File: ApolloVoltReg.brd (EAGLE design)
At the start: 45.4 x 27.3 mm, 24 parts, among them IC2 LM324D, J1 SSM-108-L-DV-BE-K-APOLLO, U1 TEXAS_INSTRUMENTS_PTH04070WAD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, U2 ACS712ELCTR-05B-T

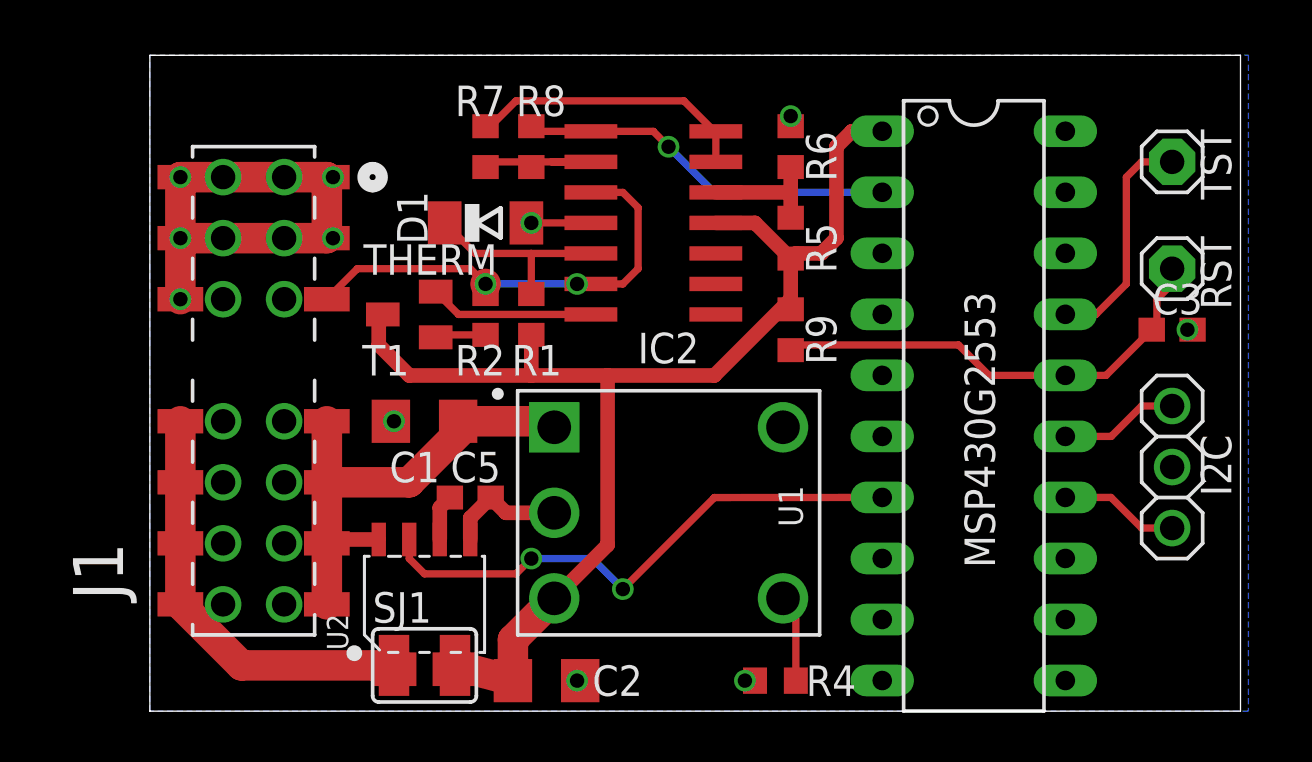
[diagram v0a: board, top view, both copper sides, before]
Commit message: pcb cleanup overtemp-shutdown (optional) gerber files
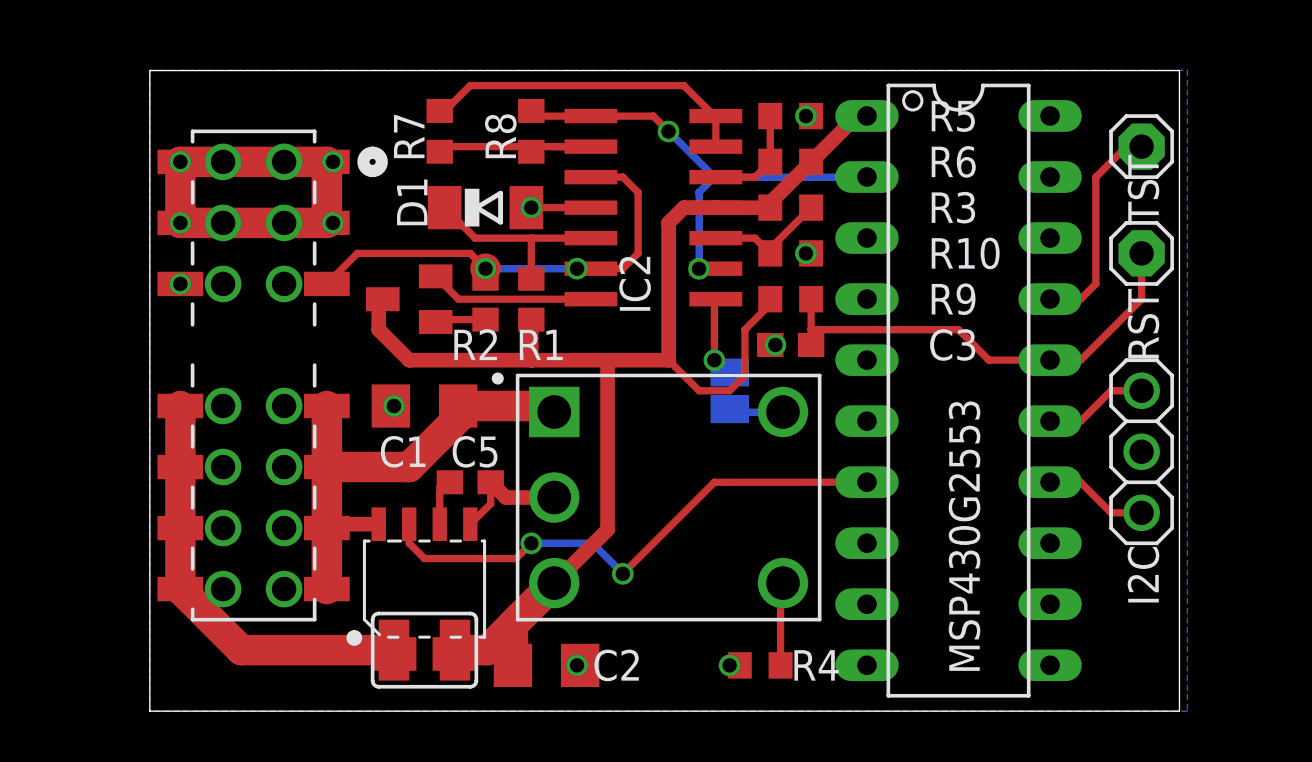
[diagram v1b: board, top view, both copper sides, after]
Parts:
- added R10, R3: 2k8, resistor:R0603
- added SJ2: (no value), jumper:SJ
- moved C3 15.9 mm to (27.9, 15.2), turned to 180 degrees
- moved R5 3.18 mm to (27.9, 22.9), turned to 180 degrees
- moved R7 2.01 mm to (13.3, 24.1)
- moved RST 1.42 mm to (42.5, 19.1)
- moved TST 1.42 mm to (42.5, 23.5)
- moved I2C 1.42 mm to (42.5, 10.8)
- moved R6 1.27 mm to (27.9, 24.8), turned to 0 degrees
- moved R9 1.27 mm to (27.9, 17.1), turned to 0 degrees
- moved MSP430G2553 0.90 mm to (34.9, 13.3)
- moved R4 0.90 mm to (26.7, 1.91)
- moved C2 0.64 mm to (17.8, 1.91)
- moved SJ1 0.64 mm to (12.7, 2.54)
- moved C1 0.63 mm to (12.7, 12.7)
- moved C5 0.63 mm to (14.6, 9.53)
- moved J1 0.63 mm to (2.54, 5.08)
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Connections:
- removed net NC: U1.5
- new net /INHIBIT: SJ2.2, U1.5
- new net N$11: IC2.3, R10.2, R3.1
- new net N$12: IC2.1, SJ2.1
- new net THERM0: J1.6
- net GND: now also R10.1; no longer J1.6
- net TEMPSENS: now also IC2.2
- net VCC: now also R3.2
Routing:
- net VCC: track 52.5 -> 59.2 mm
- net N$11: track 0.00 -> 5.14 mm
- net TEMPSENS: track 15.7 -> 19.2 mm, vias 1 -> 2
- net N$12: track 0.00 -> 3.26 mm, vias 0 -> 1
- net GND: track 27.5 -> 25.0 mm
- net /INHIBIT: track 0.00 -> 2.27 mm
- net N$8: track 6.10 -> 8.01 mm
- net N$7: track 11.8 -> 13.7 mm
- net N$6: track 5.23 -> 4.43 mm
- net SCL: track 4.97 -> 4.34 mm
- net SDA: track 4.97 -> 4.33 mm
- net N$10: track 9.68 -> 9.04 mm
- net ACS_OUT: track 23.1 -> 22.5 mm
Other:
- board size 45.4 x 27.3 mm -> 42.8 x 26.7 mm
- board text added: "Apollo 1260 3.3V/3A MC68060 switching mode voltage reg ©2019 Szymon Biegański github.com/sq7bti/ApolloVR"

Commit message: replace opamp with TL084D
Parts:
- IC2: value LM324D -> TL084D
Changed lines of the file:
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@@
 <attribute name="VALUE" x="25.4" y="2.54" size="1.27" layer="27"/>
 </element>
-<element name="IC2" library="linear" package="SO14" value="LM324D" x="22.225" y="20.955" smashed="yes" rot="R90">
+<element name="IC2" library="linear" package="SO14" value="TL084D" x="22.225" y="20.955" smashed="yes" rot="R90">
 <attribute name="NAME" x="22.098" y="16.51" size="1.27" layer="25" rot="R90"/>
 <attribute name="VALUE" x="23.622" y="16.51" size="1.27" layer="27" rot="R90"/>

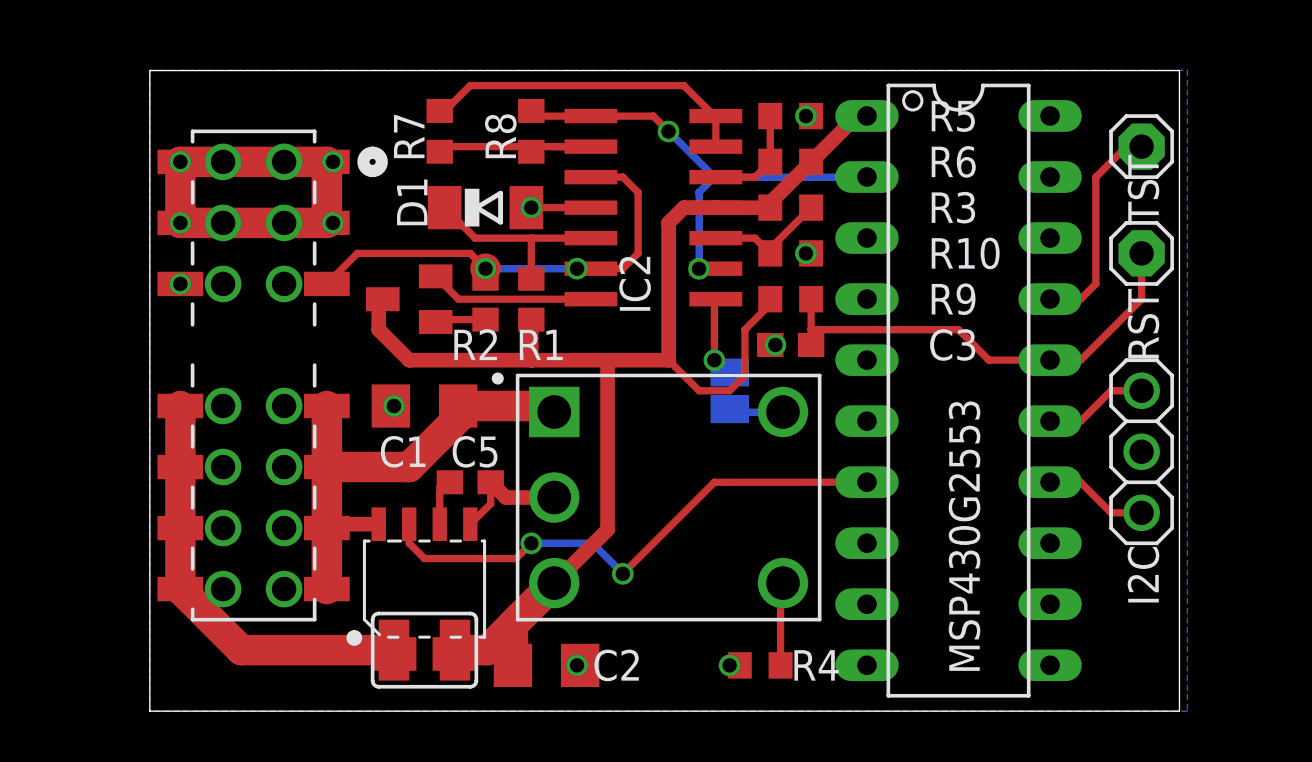
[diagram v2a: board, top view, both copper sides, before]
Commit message: widen high current traces
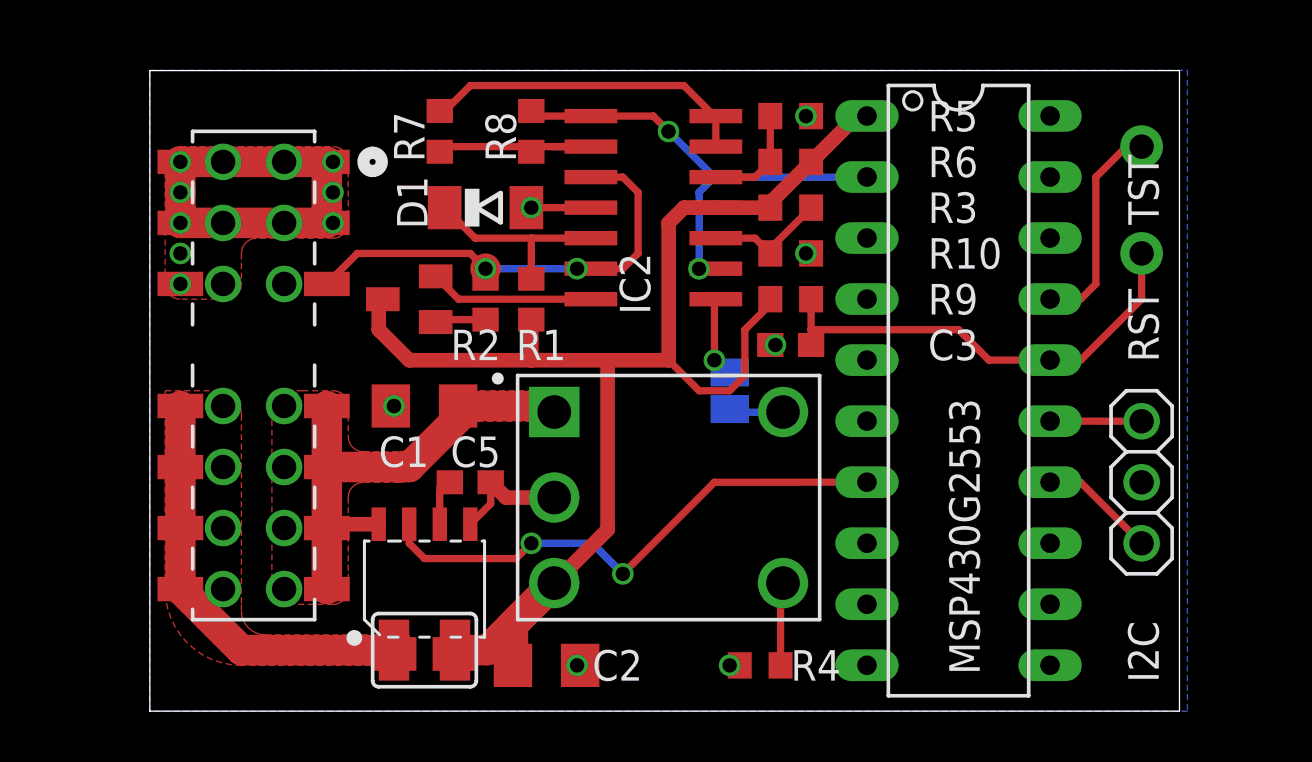
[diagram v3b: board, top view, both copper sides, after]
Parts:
- C5: value (none) -> 100n
- R10: value 2k8 -> 20k
- R2: value (none) -> 840
- R3: value 2k8 -> 2k
- RST, TST: device adafruit:1X01 -> adafruit:1X01-CLEANBIG
- moved I2C 1.27 mm to (42.5, 9.53)
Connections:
- removed net THERM0: J1.6
- net +5V: now also J1.29, J1.31, J1.33, J1.35
- net CPU: now also J1.30, J1.32, J1.34, J1.36
- net GND: now also J1.21, J1.22, J1.23, J1.24, J1.26, J1.6
- net THERM1: now also J1.25
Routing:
- net SCL: track 4.34 -> 4.86 mm
- net SDA: track 4.33 -> 3.81 mm
- net GND: vias 11 -> 15
- added copper zone on layer 1, net +5V
- added copper zone on layer 1, net CPU
- added copper zone on layer 1, net GND

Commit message: gerber in archs
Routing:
- net THERM1: track 18.6 -> 20.4 mm
- net N$8: track 8.01 -> 6.38 mm
- net VCC: track 59.2 -> 60.7 mm
- net CPU: track 17.6 -> 19.0 mm
- net N$12: track 3.26 -> 4.11 mm
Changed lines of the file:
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@@
 <grid distance="0.025" unitdist="inch" unit="inch" style="lines" multiple="1" display="yes" altdistance="0.025" altunitdist="inch" altunit="inch"/>
 <layers>
-<layer number="1" name="Top" color="4" fill="1" visible="yes" active="yes"/>
-<layer number="16" name="Bottom" color="1" fill="1" visible="yes" active="yes"/>
+<layer number="1" name="Top" color="4" fill="1" visible="no" active="yes"/>
+<layer number="16" name="Bottom" color="1" fill="1" visible="no" active="yes"/>
 <layer number="17" name="Pads" color="2" fill="1" visible="yes" active="yes"/>
 <layer number="18" name="Vias" color="2" fill="1" visible="yes" active="yes"/>
@@
 ©2019 Szymon Biegański
 github.com/sq7bti/ApolloVR</text>
+<dimension x1="1.27" y1="0" x2="44.45" y2="0" x3="22.86" y3="-3.175" textsize="1.778" layer="20" dtype="horizontal"/>
+<dimension x1="1.27" y1="0" x2="1.27" y2="26.67" x3="-1.27" y3="13.335" textsize="1.778" layer="20" dtype="horizontal"/>
 </plain>
 <attributes>
@@
 <contactref element="THERM" pad="TP"/>
 <contactref element="J1" pad="25"/>
+<wire x1="6.858" y1="17.78" x2="8.636" y2="17.78" width="0.4064" layer="1"/>
 <wire x1="19.05" y1="18.415" x2="19.625" y2="18.415" width="0" layer="19" extent="1-1"/>
-<wire x1="6.858" y1="17.78" x2="8.636" y2="17.78" width="0" layer="19" extent="1-1"/>
 </signal>
 <signal name="+5V">
@@
 <contactref element="R7" pad="2"/>
 <contactref element="R8" pad="1"/>
-<wire x1="19.625" y1="23.495" x2="17.995" y2="23.495" width="0.3048" layer="1"/>
-<wire x1="19.625" y1="23.495" x2="13.55" y2="23.495" width="0.3048" layer="1"/>
-<wire x1="13.55" y1="23.495" x2="13.335" y2="23.28" width="0.3048" layer="1"/>
-<wire x1="17.995" y1="23.495" x2="17.145" y2="23.28" width="0" layer="19" extent="1-1"/>
+<wire x1="13.335" y1="23.28" x2="17.145" y2="23.28" width="0.4064" layer="1"/>
+<wire x1="17.145" y1="23.28" x2="18.2" y2="23.28" width="0.4064" layer="1"/>
+<wire x1="18.2" y1="23.28" x2="18.415" y2="23.495" width="0.4064" layer="1"/>
+<wire x1="18.415" y1="23.495" x2="19.625" y2="23.495" width="0.4064" layer="1"/>
 </signal>
 <signal name="TEMPSENS">
@@
 <contactref element="IC2" pad="8"/>
 <contactref element="MSP430G2553" pad="2"/>
-<wire x1="19.625" y1="24.765" x2="17.36" y2="24.765" width="0.3048" layer="1"/>
-<wire x1="17.36" y1="24.765" x2="17.145" y2="24.98" width="0.3048" layer="1"/>
 <wire x1="19.625" y1="24.765" x2="22.225" y2="24.765" width="0.3048" layer="1"/>
 <wire x1="22.225" y1="24.765" x2="22.855" y2="24.125" width="0.3048" layer="1"/>
@@
 <wire x1="24.755" y1="22.225" x2="24.125" y2="21.595" width="0.3048" layer="16"/>
 <wire x1="24.125" y1="21.595" x2="24.125" y2="18.41" width="0.3048" layer="16"/>
+<wire x1="19.625" y1="24.765" x2="17.36" y2="24.765" width="0.4064" layer="1"/>
+<wire x1="17.36" y1="24.765" x2="17.145" y2="24.98" width="0.4064" layer="1"/>
 <wire x1="24.125" y1="18.41" x2="24.825" y2="18.415" width="0" layer="19" extent="1-1"/>
 </signal>
@@
 <wire x1="17.145" y1="16.295" x2="17.145" y2="14.605" width="0.6096" layer="1"/>
 <wire x1="20.32" y1="14.605" x2="22.86" y2="14.605" width="0.6096" layer="1"/>
-<wire x1="13.97" y1="2.54" x2="15.31" y2="2.54" width="1.27" layer="1"/>
-<wire x1="15.31" y1="2.54" x2="18.45" y2="5.68" width="1.27" layer="1"/>
+<wire x1="13.97" y1="2.54" x2="15.31" y2="2.54" width="1.6764" layer="1"/>
+<wire x1="15.31" y1="2.54" x2="18.45" y2="5.68" width="1.6764" layer="1"/>
 <contactref element="R3" pad="2"/>
 <wire x1="24.825" y1="20.955" x2="23.495" y2="20.955" width="0.6096" layer="1"/>
@@
 <wire x1="25.4" y1="13.335" x2="24.13" y2="13.335" width="0.3048" layer="1"/>
 <wire x1="24.13" y1="13.335" x2="22.86" y2="14.605" width="0.3048" layer="1"/>
-<wire x1="13.335" y1="2.38" x2="13.97" y2="2.54" width="0" layer="19" extent="1-1"/>
-<wire x1="14.605" y1="2.38" x2="13.97" y2="2.54" width="0" layer="19" extent="1-1"/>
+<wire x1="13.335" y1="2.38" x2="13.97" y2="2.38" width="0.4064" layer="1"/>
+<wire x1="14.605" y1="2.38" x2="13.97" y2="2.38" width="0.4064" layer="1"/>
+<wire x1="13.97" y1="2.38" x2="13.97" y2="2.54" width="0.4064" layer="1"/>
 </signal>
 <signal name="CPU">
@@
 <wire x1="2.54" y1="12.7" x2="2.54" y2="5.08" width="1.27" layer="1"/>
 <wire x1="2.54" y1="5.08" x2="5.08" y2="2.54" width="1.27" layer="1"/>
-<wire x1="5.08" y1="2.54" x2="11.43" y2="2.54" width="1.27" layer="1"/>
+<wire x1="5.08" y1="2.54" x2="11.43" y2="2.54" width="1.6764" layer="1"/>
 <polygon width="0.4064" layer="1">
 <vertex x="1.905" y="13.335"/>
@@
 <contactref element="J1" pad="34"/>
 <contactref element="J1" pad="36"/>
-<wire x1="11.43" y1="2.54" x2="10.795" y2="2.38" width="0" layer="19" extent="1-1"/>
-<wire x1="12.065" y1="2.38" x2="11.43" y2="2.54" width="0" layer="19" extent="1-1"/>
+<wire x1="10.795" y1="2.38" x2="11.43" y2="2.38" width="0.4064" layer="1"/>
+<wire x1="12.065" y1="2.38" x2="11.43" y2="2.38" width="0.4064" layer="1"/>
+<wire x1="11.43" y1="2.38" x2="11.43" y2="2.54" width="0.4064" layer="1"/>
 </signal>
 <signal name="N$9">
@@
 <wire x1="24.765" y1="14.605" x2="24.765" y2="17.085" width="0.3048" layer="1"/>
 <wire x1="24.765" y1="17.085" x2="24.825" y2="17.145" width="0.3048" layer="1"/>
-<wire x1="24.765" y1="14.605" x2="25.4" y2="14.097" width="0" layer="19" extent="16-16"/>
+<wire x1="25.4" y1="14.097" x2="25.273" y2="14.097" width="0.4064" layer="16"/>
+<wire x1="25.273" y1="14.097" x2="24.765" y2="14.605" width="0.4064" layer="16"/>
 </signal>
 </signals>

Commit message: adding pic
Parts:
- removed T1: (no value), transistor:SOT23-EBC
- added D2: BAS40-06, diode:SOT23
- added FAN: (no value), pinhead:1X02
- added IC1: MCP1703CB, linear:SOT23
- added LED1: (no value), adafruit:LED3MM
- added Q1: (no value), semicon-smd-ipc:SOT23
- added Q2: (no value), adafruit:SOT23
- added R11, R12, R13: 2k, resistor:R0805
- added R14: 2k, resistor:R0603
- added SJ3, SJ5: (no value), jumper:SJ_2
- C1, C2: device eagle-ltspice:C1206 -> eagle-ltspice:C1210
- D1: value (none) -> BAS40-04; device diode:SOD80C -> diode:SOT23
- I2C: device adafruit:1X03 -> pinhead:1X05
- R1: value 121 -> 1k; device resistor:R0603 -> resistor:R0805
- R10, R3, R4, R5, R6, R7, R8: device resistor:R0603 -> resistor:R0805
- R2: value 840 -> 1k3; device resistor:R0603 -> resistor:R0805
- moved R1 10.8 mm to (9.53, 24.8), turned to 180 degrees
- moved R9 7.85 mm to (35.6, 15.2), flipped to the bottom, turned to 180 degrees
- moved C3 7.73 mm to (35.6, 14.0), flipped to the bottom, turned to 0 degrees
- moved D1 7.65 mm to (10.2, 15.2), turned to 270 degrees
- moved THERM 6.87 mm to (21.0, 22.2)
- moved TST 5.08 mm to (42.5, 18.4)
- moved RST 3.18 mm to (42.5, 15.9)
- moved C5 2.01 mm to (14.0, 7.62), flipped to the bottom, turned to 0 degrees
- moved R3 1.90 mm to (27.9, 19.1), turned to 0 degrees
- moved I2C 1.27 mm to (42.5, 8.26)
- moved C1 0.90 mm to (12.1, 12.1), turned to 90 degrees
- moved R8 0.90 mm to (16.5, 24.8), turned to 0 degrees
- moved R2 0.90 mm to (14.6, 16.5)
- moved R7 0.64 mm to (13.3, 24.8), turned to 0 degrees
- moved R4 0.63 mm to (27.3, 1.91)
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- renumbered MSP430G2553 to JLCJLCJLCJLC
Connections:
- net N$9 renamed RST
- new net N$13: IC2.13, R11.2, R14.2
- new net N$14: IC2.14, R11.1, SJ3.1
- new net N$15: JLCJLCJLCJLC.7, SJ3.2
- new net N$16: IC1.2, JLCJLCJLCJLC.1, R9.1, SJ5.2
- new net N$17: D2.2, IC2.1
- new net N$18: D2.3, SJ2.1
- new net N$19: FAN.2, Q2.3
- new net N$21: I2C.3, SJ5.3
- new net N$9: JLCJLCJLCJLC.19, Q2.1
- net +5V: now also FAN.1, IC1.3, IC2.4, LED1.A, R12.1, R2.2, R3.2, R5.1
- net ACS_OUT: now also R14.1, SJ3.3; no longer JLCJLCJLCJLC.7
- net CPU: now also D1.2
- net GND: now also D1.1, I2C.1, I2C.5, IC1.1, Q2.2, R1.2, R13.2; no longer D1.A, I2C.2
- net N$12: now also D2.1, JLCJLCJLCJLC.5; no longer IC2.1, SJ2.1
- net N$2: now also LED1.K, Q1.1, R1.1; no longer D1.C, IC2.12, R1.2
- net N$3: now also Q1.2, R2.1; no longer IC2.14, T1.B
- net N$4: now also IC2.12, R12.2, R13.1; no longer R2.2, T1.E
- net SCL: now also I2C.4; no longer I2C.3
- net SDA: now also I2C.2; no longer I2C.1
- net THERM1: now also D1.3, Q1.3; no longer IC2.13, R2.1
- net VCC: now also SJ5.1; no longer IC2.4, JLCJLCJLCJLC.1, R1.1, R3.2, R5.1, R9.1, T1.C
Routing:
- net +5V: track 21.1 -> 76.3 mm, vias 0 -> 1
- net VCC: track 60.7 -> 27.2 mm, vias 0 -> 1
- net N$16: track 0.00 -> 26.9 mm, vias 0 -> 3
- net N$13: track 0.00 -> 11.4 mm, vias 0 -> 1
- net RST: track 19.1 -> 7.93 mm
- net N$14: track 0.00 -> 10.6 mm, vias 0 -> 1
- net N$21: track 0.00 -> 9.05 mm, vias 0 -> 1
- net N$19: track 0.00 -> 8.93 mm
- net N$15: track 0.00 -> 8.52 mm
- net ACS_OUT: track 22.5 -> 14.1 mm, vias 2 -> 1
- net CPU: track 19.0 -> 26.9 mm
- net GND: track 25.0 -> 31.8 mm, vias 15 -> 60
- net N$10: track 9.04 -> 4.33 mm
- net N$9: track 0.00 -> 3.69 mm
- net N$18: track 0.00 -> 3.07 mm, vias 0 -> 1
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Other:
- board size 42.8 x 26.7 mm -> 44.1 x 26.7 mm
